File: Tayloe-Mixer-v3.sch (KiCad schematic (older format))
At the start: 60 parts, among them J1 BNC, J101 Audio_Jack, J3 Jack-DC, J4 Conn_01x07_Female, Q1 2N3904-SMD, Q2 2N3904-SMD, SW1 SW_DIP_x01, SW2 Rotary_Encoder_Switch, T1 6:31, T2 31:6, T3 T50_SPLITTER, U1 ESP32-A1S, U2 FST3253, U201 MAR6, U3 LM4562, U4 si5351, U5 L7805, U7 AMS1117CD-3.3

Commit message: rerouting
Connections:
- wire segments 211 -> 217
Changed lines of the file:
@@
 Connection ~ 4100 2650
 Connection ~ 4400 2650
-Wire Wire Line
-	10350 4250 11100 4250
-Wire Wire Line
-	11100 4250 11100 4150
-Wire Wire Line
-	11100 4150 11750 4150
-Wire Wire Line
-	11750 4550 11100 4550
-Wire Wire Line
-	11100 4550 11100 4450
-Wire Wire Line
-	11100 4450 10350 4450
 $Comp
 L Tayloe-Mixer-v2-rescue:BNC-Xenir J1
@@
 	-1   0    0    1
 $EndComp
-Wire Wire Line
-	4200 8450 5150 8450
-Wire Wire Line
-	4200 8650 5150 8650
 $Comp
 L power:GND #PWR0111
@@
 Wire Wire Line
 	3400 8100 4650 8100
-Wire Wire Line
-	4650 8100 4650 8250
-Wire Wire Line
-	4650 8250 5150 8250
 Text GLabel 7500 9250 2    50   Input ~ 0
 Q_SIGNAL
@@
 	1    0    0    -1
 $EndComp
+Wire Wire Line
+	10900 4150 10900 4450
+Wire Wire Line
+	10900 4450 10350 4450
+Wire Wire Line
+	10900 4150 11750 4150
+Wire Wire Line
+	11000 4550 11000 4250
+Wire Wire Line
+	11000 4250 10350 4250
+Wire Wire Line
+	11000 4550 11750 4550
+Text GLabel 5150 8050 0    50   Input ~ 0
+IO0
+Wire Wire Line
+	4650 8650 5150 8650
+Wire Wire Line
+	4650 8100 4650 8650
+Wire Wire Line
+	4550 8650 4200 8650
+Wire Wire Line
+	4200 8450 4800 8450
+Wire Wire Line
+	4800 8450 4800 8250
+Wire Wire Line
+	4800 8250 5150 8250
+Wire Wire Line
+	5150 8450 4900 8450
+Wire Wire Line
+	4900 8450 4900 8550
+Wire Wire Line
+	4900 8550 4550 8550
+Wire Wire Line
+	4550 8550 4550 8650
 $EndSCHEMATC

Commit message: finished?
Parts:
- removed D1: LCD_I2C, xenir:LCD_I2C, symbol xenir:LCD_I2C
- added J2: Conn_01x04, Connector_PinSocket_2.54mm:PinSocket_1x04_P2.54mm_Vertical, symbol Connector_Generic:Conn_01x04
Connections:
- net labels added: 2.5V
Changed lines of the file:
@@
 	10550 2850 11000 2850
-$Comp
-L xenir:LCD_I2C D1
-U 1 1 62B0F410
-P 9450 9750
-F 0 "D1" H 9728 8696 50  0000 L CNN
-F 1 "LCD_I2C" H 9728 8605 50  0000 L CNN
-F 2 "xenir:LCD_I2C" H 9450 9750 50  0001 C CNN
-F 3 "" H 9450 9750 50  0001 C CNN
-	1    9450 9750
-	0    1    1    0
-$EndComp
 $Comp
 L power:+5V #PWR013
@@
 Wire Wire Line
 	4550 8550 4550 8650
+Text GLabel 8850 2550 1    50   Input ~ 0
+2.5V
+$Comp
+L Connector_Generic:Conn_01x04 J2
+U 1 1 63904F29
+P 9000 9600
+F 0 "J2" V 8872 9780 50  0000 L CNN
+F 1 "Conn_01x04" V 8963 9780 50  0000 L CNN
+F 2 "Connector_PinSocket_2.54mm:PinSocket_1x04_P2.54mm_Vertical" H 9000 9600 50  0001 C CNN
+F 3 "~" H 9000 9600 50  0001 C CNN
+	1    9000 9600
+	0    1    1    0
+$EndComp
 $EndSCHEMATC

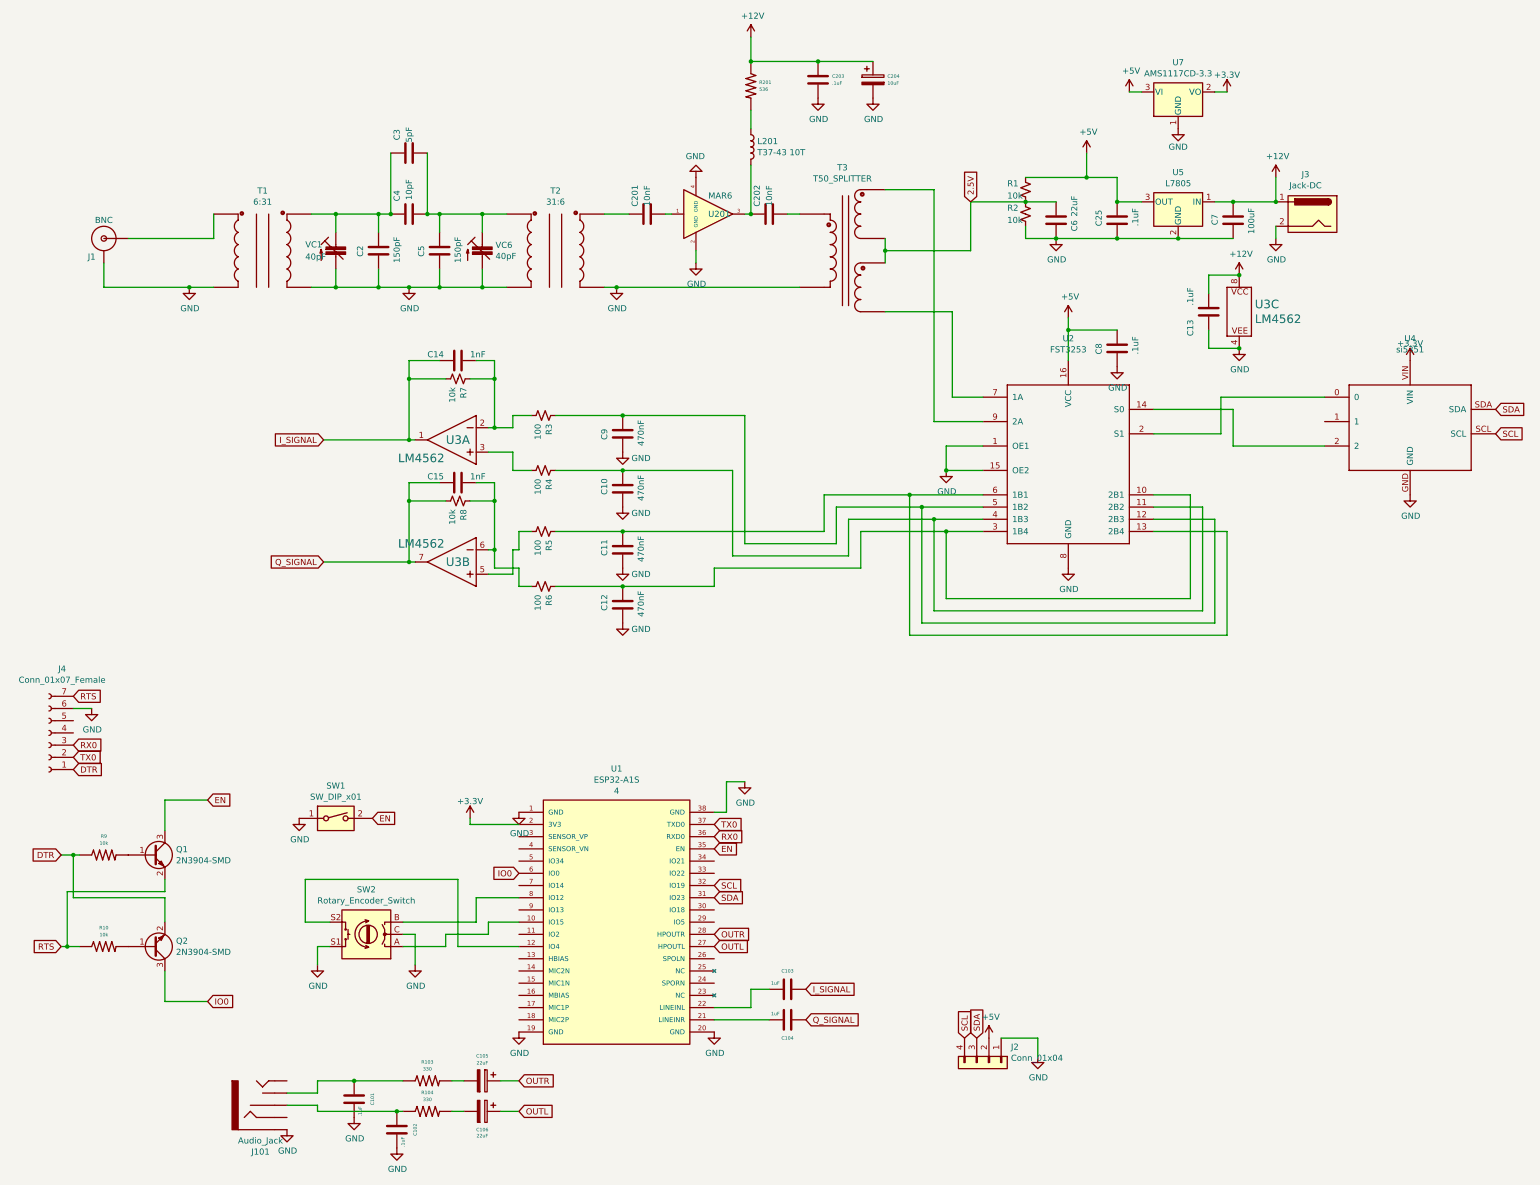
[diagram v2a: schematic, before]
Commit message: fixed audio jack
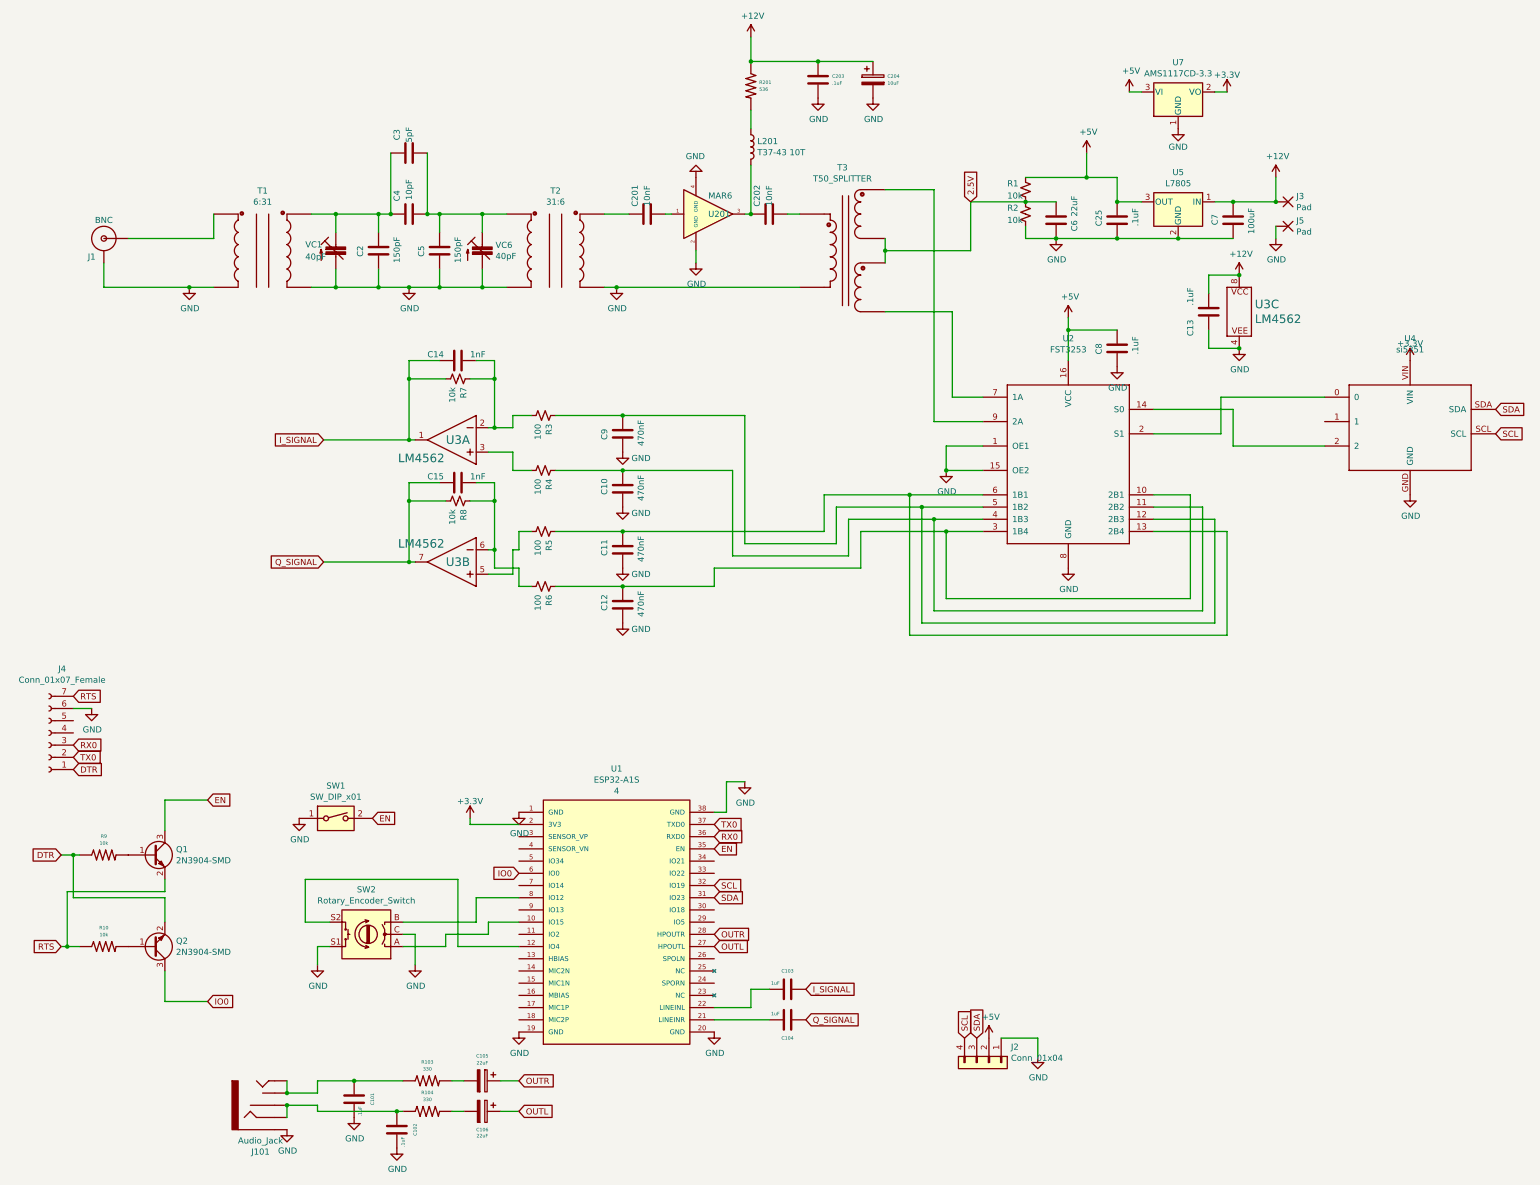
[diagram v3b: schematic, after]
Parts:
- removed J3: Jack-DC, Connector_BarrelJack:BarrelJack_Horizontal, symbol Connector:Jack-DC
- added J3, J5: Pad, Xenir:Pad, symbol xenir:Pad
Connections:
- net +12V: now also J3.1 (P)
- net GND: now also J5.1 (P)
- net at J101.RING: now also C102.1, J101.RSH, R104.1
- net at J101.TIP: now also C101.1, J101.TSH, R103.1
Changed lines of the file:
@@
 	2250 8850 2250 9100
-$Comp
-L Connector:Jack-DC J3
-U 1 1 633DF648
-P 11650 2650
-F 0 "J3" H 11707 2975 50  0000 C CNN
-F 1 "Jack-DC" H 11707 2884 50  0000 C CNN
-F 2 "Connector_BarrelJack:BarrelJack_Horizontal" H 11700 2610 50  0001 C CNN
-F 3 "~" H 11700 2610 50  0001 C CNN
-	1    11650 2650
-	-1   0    0    -1
-$EndComp
-Connection ~ 11350 2550
 $Comp
 L power:GND #PWR0114
@@
 	0    1    1    0
 $EndComp
+$Comp
+L xenir:Pad J3
+U 1 1 6394DBBE
+P 11450 2700
+F 0 "J3" H 11382 2504 50  0000 R CNN
+F 1 "Pad" H 11382 2595 50  0000 R CNN
+F 2 "Xenir:Pad" H 11450 2700 50  0001 C CNN
+F 3 "" H 11450 2700 50  0001 C CNN
+	1    11450 2700
+	-1   0    0    1
+$EndComp
+Connection ~ 11350 2550
+$Comp
+L xenir:Pad J5
+U 1 1 6394E321
+P 11450 2900
+F 0 "J5" H 11382 2704 50  0000 R CNN
+F 1 "Pad" H 11382 2795 50  0000 R CNN
+F 2 "Xenir:Pad" H 11450 2900 50  0001 C CNN
+F 3 "" H 11450 2900 50  0001 C CNN
+	1    11450 2900
+	-1   0    0    1
+$EndComp
+Wire Wire Line
+	3250 9750 3250 9850
+Connection ~ 3250 9850
+Wire Wire Line
+	3250 10050 3250 9950
+Connection ~ 3250 9950
 $EndSCHEMATC

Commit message: gg
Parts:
- C101, C102, C103, C104: symbol xenir:Capacitor -> Tayloe-Mixer-v3-rescue:Capacitor-xenir
- C105, C106: symbol xenir:Cap_Polarized -> Tayloe-Mixer-v3-rescue:Cap_Polarized-xenir
- J101: symbol xenir:Audio_Jack -> Tayloe-Mixer-v3-rescue:Audio_Jack-xenir
- J3, J5: symbol xenir:Pad -> Tayloe-Mixer-v3-rescue:Pad-xenir
- Q1, Q2: symbol xenir:2N3904-SMD -> Tayloe-Mixer-v3-rescue:2N3904-SMD-xenir
- R10, R9: symbol esp32-a1s-rescue:Resistor-Xenir -> Tayloe-Mixer-v3-rescue:Resistor-Xenir-esp32-a1s-rescue
- R103, R104: symbol xenir:Resistor -> Tayloe-Mixer-v3-rescue:Resistor-xenir
- U1: symbol xenir:ESP32-A1S -> Tayloe-Mixer-v3-rescue:ESP32-A1S-xenir
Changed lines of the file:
@@
 I_SIGNAL
 $Comp
-L xenir:Capacitor C103
+L Tayloe-Mixer-v3-rescue:Capacitor-xenir C103
 U 1 1 62B36FA7
 P 7350 9000
@@
 $EndComp
 $Comp
-L xenir:Capacitor C104
+L Tayloe-Mixer-v3-rescue:Capacitor-xenir C104
 U 1 1 62B37510
 P 7350 9250
@@
 OUTR
 $Comp
-L xenir:Audio_Jack J101
+L Tayloe-Mixer-v3-rescue:Audio_Jack-xenir J101
 U 1 1 62B4F5DF
 P 3050 10300
@@
 $EndComp
 $Comp
-L xenir:Capacitor C101
+L Tayloe-Mixer-v3-rescue:Capacitor-xenir C101
 U 1 1 62B508AF
 P 3800 9900
@@
 $EndComp
 $Comp
-L xenir:Capacitor C102
+L Tayloe-Mixer-v3-rescue:Capacitor-xenir C102
 U 1 1 62B50F6B
 P 4150 10150
@@
 $EndComp
 $Comp
-L xenir:Resistor R103
+L Tayloe-Mixer-v3-rescue:Resistor-xenir R103
 U 1 1 62B531E9
 P 4400 9750
@@
 $EndComp
 $Comp
-L xenir:Resistor R104
+L Tayloe-Mixer-v3-rescue:Resistor-xenir R104
 U 1 1 62B53AF7
 P 4400 10000
@@
 $EndBitmap
 $Comp
-L xenir:ESP32-A1S U1
+L Tayloe-Mixer-v3-rescue:ESP32-A1S-xenir U1
 U 1 1 62B0B8E9
 P 5950 8450
@@
 $EndComp
 $Comp
-L xenir:Cap_Polarized C105
+L Tayloe-Mixer-v3-rescue:Cap_Polarized-xenir C105
 U 1 1 62CE938D
 P 4850 9850
@@
 $EndComp
 $Comp
-L xenir:Cap_Polarized C106
+L Tayloe-Mixer-v3-rescue:Cap_Polarized-xenir C106
 U 1 1 62CEA988
 P 4850 10100
@@
 SDA
 $Comp
-L xenir:2N3904-SMD Q1
+L Tayloe-Mixer-v3-rescue:2N3904-SMD-xenir Q1
 U 1 1 63749133
 P 2250 7750
@@
 	2250 7450 2600 7450
 $Comp
-L esp32-a1s-rescue:Resistor-Xenir R9
+L Tayloe-Mixer-v3-rescue:Resistor-Xenir-esp32-a1s-rescue R9
 U 1 1 637D5201
 P 1750 7900
@@
 	1400 7900 1500 7900
 $Comp
-L esp32-a1s-rescue:Resistor-Xenir R10
+L Tayloe-Mixer-v3-rescue:Resistor-Xenir-esp32-a1s-rescue R10
 U 1 1 63814A82
 P 1750 8650
@@
 	1400 8650 1450 8650
 $Comp
-L xenir:2N3904-SMD Q2
+L Tayloe-Mixer-v3-rescue:2N3904-SMD-xenir Q2
 U 1 1 63824306
 P 2250 8800
@@
 $EndComp
 $Comp
-L xenir:Pad J3
+L Tayloe-Mixer-v3-rescue:Pad-xenir J3
 U 1 1 6394DBBE
 P 11450 2700
@@
 Connection ~ 11350 2550
 $Comp
-L xenir:Pad J5
+L Tayloe-Mixer-v3-rescue:Pad-xenir J5
 U 1 1 6394E321
 P 11450 2900
